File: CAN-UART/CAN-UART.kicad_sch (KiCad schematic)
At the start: 13 parts, among them P1 USB_C_Plug_USB2.0, U1 AP2112K-3.3, U2 SN65HVD230

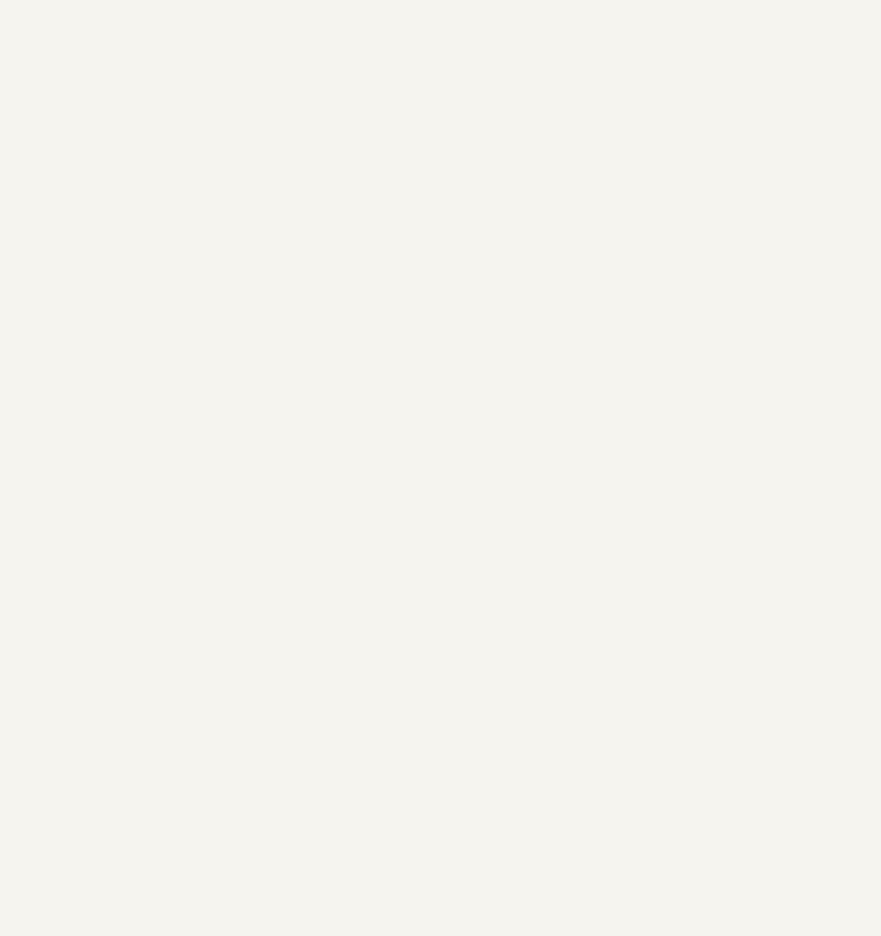
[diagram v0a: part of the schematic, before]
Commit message: Added ESP32 C3
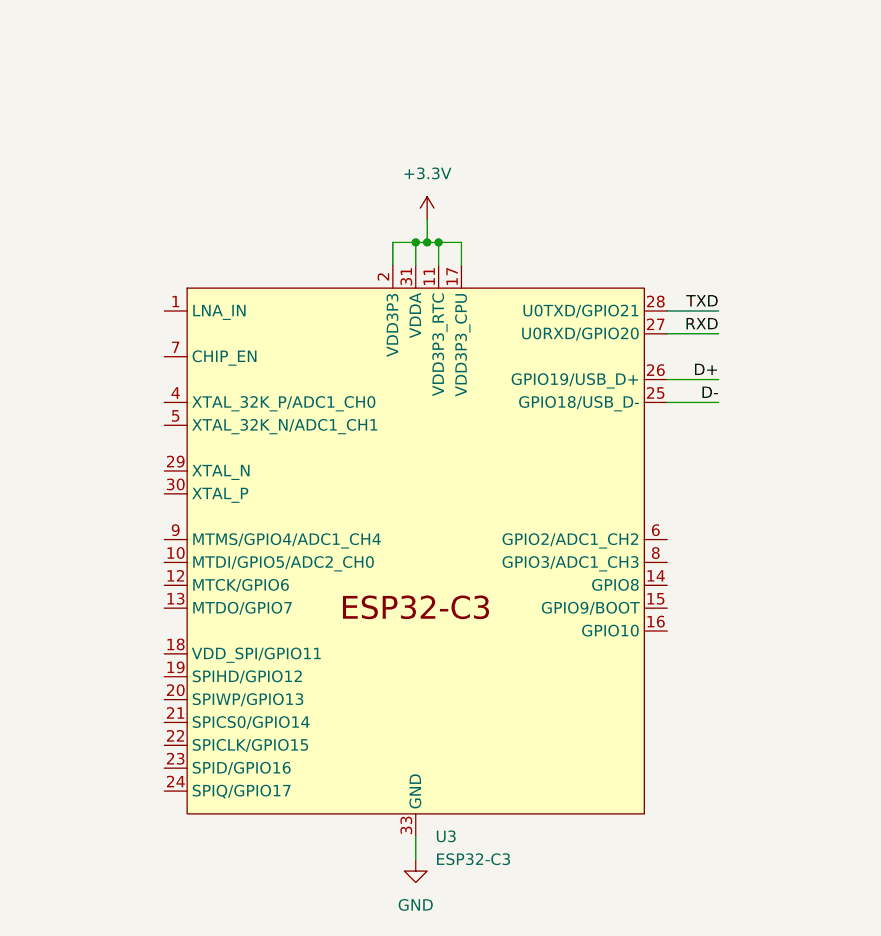
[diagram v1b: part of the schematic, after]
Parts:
- added U3: ESP32-C3, Package_DFN_QFN:QFN-32-1EP_5x5mm_P0.5mm_EP3.45x3.45mm, symbol Espressif:ESP32-C3
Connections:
- net D+: now also U3.26 (GPIO19/USB_D+)
- net D-: now also U3.25 (GPIO18/USB_D-)
- net GND: now also U3.33 (GND)
- new net +3.3V: U3.11 (VDD3P3_RTC), U3.17 (VDD3P3_CPU), U3.2 (VDD3P3), U3.3 (VDD3P3), U3.31 (VDDA), U3.32 (VDDA)
- new net RXD: U3.27 (U0RXD/GPIO20)
- new net TXD: U3.28 (U0TXD/GPIO21)
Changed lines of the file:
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@@
   (junction (at 144.78 24.13) (diameter 0) (color 0 0 0 0)
   )
+  (junction (at 120.65 96.52) (diameter 0) (color 0 0 0 0)
+  )
   (junction (at 99.06 45.72) (diameter 0) (color 0 0 0 0)
   )
@@
   (junction (at 88.9 33.02) (diameter 0) (color 0 0 0 0)
   )
+  (junction (at 121.92 96.52) (diameter 0) (color 0 0 0 0)
+  )
   (junction (at 115.57 45.72) (diameter 0) (color 0 0 0 0)
+  )
+  (junction (at 123.19 96.52) (diameter 0) (color 0 0 0 0)
   )
   (no_connect (at 322.58 104.14))
@@
     (stroke (width 0) (type default))
   )
+  (wire (pts (xy 120.65 96.52) (xy 120.65 99.06))
+    (stroke (width 0) (type default))
+  )
   (wire (pts (xy 340.36 109.22) (xy 340.36 111.76))
     (stroke (width 0) (type default))
@@
     (stroke (width 0) (type default))
   )
+  (wire (pts (xy 148.59 104.14) (xy 154.305 104.14))
+    (stroke (width 0) (type default))
+  )
+  (wire (pts (xy 118.11 96.52) (xy 120.65 96.52))
+    (stroke (width 0) (type default))
+  )
+  (wire (pts (xy 118.11 99.06) (xy 118.11 96.52))
+    (stroke (width 0) (type default))
+  )
   (wire (pts (xy 67.31 36.83) (xy 64.77 36.83))
     (stroke (width 0) (type default))
@@
     (stroke (width 0) (type default))
   )
+  (wire (pts (xy 123.19 96.52) (xy 123.19 99.06))
+    (stroke (width 0) (type default))
+  )
   (wire (pts (xy 106.68 33.02) (xy 115.57 33.02))
     (stroke (width 0) (type default))
@@
     (stroke (width 0) (type default))
   )
+  (wire (pts (xy 148.59 111.76) (xy 154.305 111.76))
+    (stroke (width 0) (type default))
+  )
   (wire (pts (xy 350.52 99.06) (xy 353.06 99.06))
     (stroke (width 0) (type default))
@@
     (stroke (width 0) (type default))
   )
+  (wire (pts (xy 120.65 96.52) (xy 121.92 96.52))
+    (stroke (width 0) (type default))
+  )
+  (wire (pts (xy 123.19 96.52) (xy 125.73 96.52))
+    (stroke (width 0) (type default))
+  )
   (wire (pts (xy 156.21 30.48) (xy 144.78 30.48))
     (stroke (width 0) (type default))
   )
+  (wire (pts (xy 125.73 96.52) (xy 125.73 99.06))
+    (stroke (width 0) (type default))
+  )
   (wire (pts (xy 67.31 36.83) (xy 67.31 39.37))
     (stroke (width 0) (type default))
@@
     (stroke (width 0) (type default))
   )
+  (wire (pts (xy 148.59 114.3) (xy 154.305 114.3))
+    (stroke (width 0) (type default))
+  )
   (wire (pts (xy 322.58 101.6) (xy 330.2 101.6))
     (stroke (width 0) (type default))
@@
     (stroke (width 0) (type default))
   )
+  (wire (pts (xy 120.65 162.56) (xy 120.65 165.1))
+    (stroke (width 0) (type default))
+  )
+  (wire (pts (xy 121.92 96.52) (xy 123.19 96.52))
+    (stroke (width 0) (type default))
+  )
   (wire (pts (xy 88.9 35.56) (xy 88.9 33.02))
     (stroke (width 0) (type default))
   )
+  (wire (pts (xy 148.59 106.68) (xy 154.305 106.68))
+    (stroke (width 0) (type default))
+  )
   (wire (pts (xy 115.57 25.4) (xy 115.57 33.02))
+    (stroke (width 0) (type default))
+  )
+  (wire (pts (xy 121.92 93.98) (xy 121.92 96.52))
     (stroke (width 0) (type default))
   )
@@
     (effects (font (size 2.54 2.54)) (justify left bottom))
   )
+  (label "D-" (at 154.305 114.3 180) (fields_autoplaced)
+    (effects (font (size 1.27 1.27)) (justify right bottom))
+  )
   (label "CAN_RX" (at 322.58 99.06 0) (fields_autoplaced)
     (effects (font (size 1.27 1.27)) (justify left bottom))
   )
   (label "D+" (at 57.15 49.53 180) (fields_autoplaced)
+    (effects (font (size 1.27 1.27)) (justify right bottom))
+  )
+  (label "RXD" (at 154.305 106.68 180) (fields_autoplaced)
+    (effects (font (size 1.27 1.27)) (justify right bottom))
+  )
+  (label "TXD" (at 154.305 104.14 180) (fields_autoplaced)
+    (effects (font (size 1.27 1.27)) (justify right bottom))
+  )
+  (label "D+" (at 154.305 111.76 180) (fields_autoplaced)
     (effects (font (size 1.27 1.27)) (justify right bottom))
   )
@@
     )
   )
+  (symbol (lib_id "Espressif:ESP32-C3") (at 120.65 132.08 0) (unit 1)
+    (in_bom yes) (on_board yes) (dnp no) (fields_autoplaced)
+    (property "Reference" "U3" (at 122.8441 162.56 0)
+      (effects (font (size 1.27 1.27)) (justify left))
+    )
+    (property "Value" "ESP32-C3" (at 122.8441 165.1 0)
+      (effects (font (size 1.27 1.27)) (justify left))
+    )
+    (property "Footprint" "Package_DFN_QFN:QFN-32-1EP_5x5mm_P0.5mm_EP3.45x3.45mm" (at 120.65 170.18 0)
+      (effects (font (size 1.27 1.27)) hide)
+    )
+    (property "Datasheet" "https://www.espressif.com/sites/default/files/documentation/esp32-c3_datasheet_en.pdf" (at 120.65 172.72 0)
+      (effects (font (size 1.27 1.27)) hide)
+    )
+    (pin "1")
+    (pin "10")
+    (pin "11")
+    (pin "12")
+    (pin "13")
+    (pin "14")
+    (pin "15")
+    (pin "16")
+    (pin "17")
+    (pin "18")
+    (pin "19")
+    (pin "2")
+    (pin "20")
+    (pin "21")
+    (pin "22")
+    (pin "23")
+    (pin "24")
+    (pin "25")
+    (pin "26")
+    (pin "27")
+    (pin "28")
+    (pin "29")
+    (pin "30")
+    (pin "31")
+    (pin "33")
+    (pin "4")
+    (pin "5")
+    (pin "6")
+    (pin "7")
+    (pin "8")
+    (pin "9")
+    (pin "3")
+    (pin "32")
+    (instances
+      (project "CAN-UART"
+        (path "/21020eba-b649-4135-9bee-384d0a5cab58"
+          (reference "U3") (unit 1)
+        )
+      )
+    )
+  )
   (symbol (lib_id "Interface_CAN_LIN:SN65HVD230") (at 340.36 99.06 0) (unit 1)
     (in_bom yes) (on_board yes) (dnp no) (fields_autoplaced)
@@
         )
       )
+    )
+  )
+  (symbol (lib_name "GND_1") (lib_id "power:GND") (at 120.65 165.1 0) (unit 1)
+    (in_bom yes) (on_board yes) (dnp no) (fields_autoplaced)
+    (property "Reference" "#PWR010" (at 120.65 171.45 0)
+      (effects (font (size 1.27 1.27)) hide)
+    )
+    (property "Value" "GND" (at 120.65 170.18 0)
+      (effects (font (size 1.27 1.27)))
+    )
+    (property "Footprint" "" (at 120.65 165.1 0)
+      (effects (font (size 1.27 1.27)) hide)
+    )
+    (property "Datasheet" "" (at 120.65 165.1 0)
+      (effects (font (size 1.27 1.27)) hide)
+    )
+    (pin "1")
+    (instances
+      (project "CAN-UART"
+        (path "/21020eba-b649-4135-9bee-384d0a5cab58"
+          (reference "#PWR010") (unit 1)
+        )
+      )
+    )
+  )
+  (symbol (lib_id "power:+3.3V") (at 121.92 93.98 0) (unit 1)
+    (in_bom yes) (on_board yes) (dnp no) (fields_autoplaced)
+    (property "Reference" "#PWR07" (at 121.92 97.79 0)
+      (effects (font (size 1.27 1.27)) hide)
+    )
+    (property "Value" "+3.3V" (at 121.92 88.9 0)
+      (effects (font (size 1.27 1.27)))
+    )
+    (property "Footprint" "" (at 121.92 93.98 0)
+      (effects (font (size 1.27 1.27)) hide)
+    )
+    (property "Datasheet" "" (at 121.92 93.98 0)
+      (effects (font (size 1.27 1.27)) hide)
+    )
+    (pin "1")
+    (instances
+      (project "CAN-UART"
+        (path "/21020eba-b649-4135-9bee-384d0a5cab58"
+          (reference "#PWR07") (unit 1)
+        )
+      )

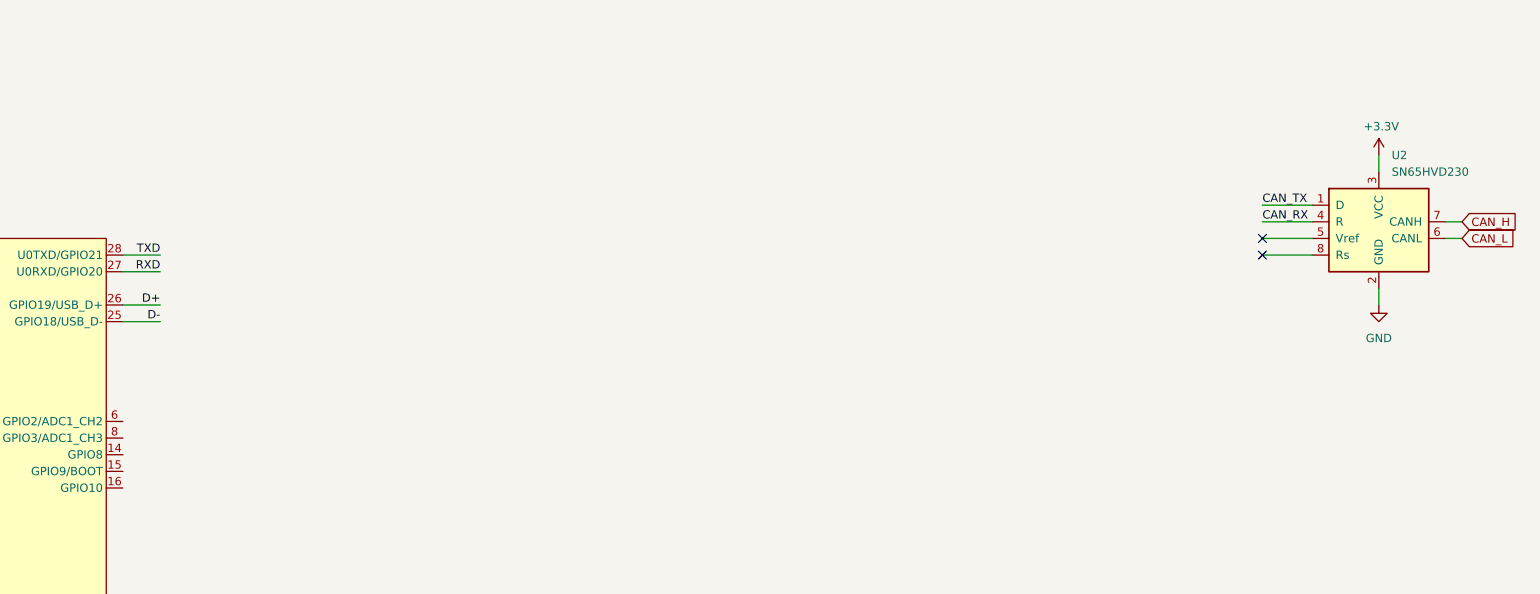
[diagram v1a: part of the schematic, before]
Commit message: Added SN65HVD230 Transceiver
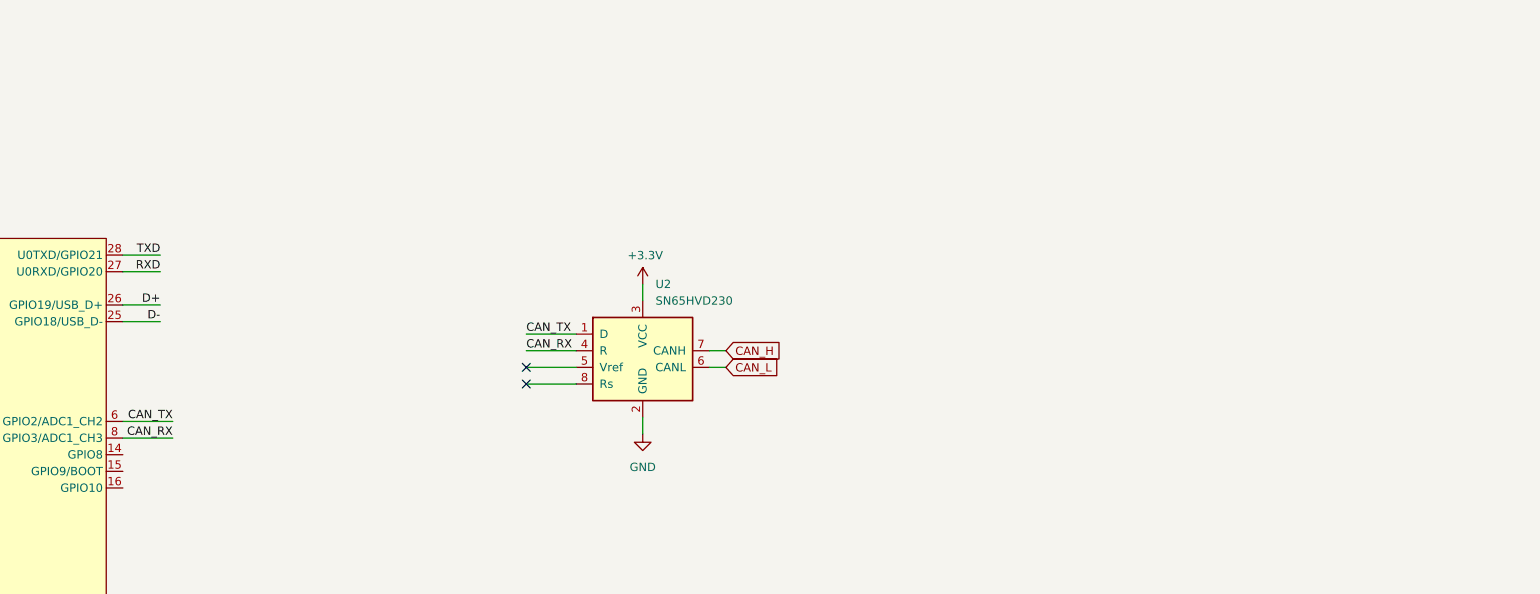
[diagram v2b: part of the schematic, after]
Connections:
- net CAN_RX: now also U3.8 (GPIO3/ADC1_CH3)
- net CAN_TX: now also U3.6 (GPIO2/ADC1_CH2)
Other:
- moved on the sheet: U2
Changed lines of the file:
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@@
   (junction (at 123.19 96.52) (diameter 0) (color 0 0 0 0)
   )
-  (no_connect (at 322.58 104.14))
+  (no_connect (at 210.185 123.825))
   (no_connect (at 57.15 39.37))
-  (no_connect (at 322.58 101.6))
+  (no_connect (at 210.185 121.285))
   (wire (pts (xy 139.7 24.13) (xy 139.7 30.48))
     (stroke (width 0) (type default))
   )
-  (wire (pts (xy 322.58 99.06) (xy 330.2 99.06))
+  (wire (pts (xy 210.185 118.745) (xy 217.805 118.745))
     (stroke (width 0) (type default))
   )
@@
     (stroke (width 0) (type default))
   )
+  (wire (pts (xy 156.21 129.54) (xy 148.59 129.54))
+    (stroke (width 0) (type default))
+  )
   (wire (pts (xy 52.07 36.83) (xy 57.15 36.83))
     (stroke (width 0) (type default))
@@
     (stroke (width 0) (type default))
   )
-  (wire (pts (xy 340.36 109.22) (xy 340.36 111.76))
-    (stroke (width 0) (type default))
-  )
-  (wire (pts (xy 340.36 88.9) (xy 340.36 91.44))
+  (wire (pts (xy 227.965 128.905) (xy 227.965 131.445))
+    (stroke (width 0) (type default))
+  )
+  (wire (pts (xy 227.965 108.585) (xy 227.965 111.125))
     (stroke (width 0) (type default))
   )
@@
     (stroke (width 0) (type default))
   )
+  (wire (pts (xy 156.21 132.08) (xy 148.59 132.08))
+    (stroke (width 0) (type default))
+  )
   (wire (pts (xy 36.83 72.39) (xy 36.83 69.85))
     (stroke (width 0) (type default))
   )
-  (wire (pts (xy 350.52 101.6) (xy 353.06 101.6))
+  (wire (pts (xy 238.125 121.285) (xy 240.665 121.285))
     (stroke (width 0) (type default))
   )
@@
     (stroke (width 0) (type default))
   )
-  (wire (pts (xy 322.58 104.14) (xy 330.2 104.14))
+  (wire (pts (xy 210.185 123.825) (xy 217.805 123.825))
     (stroke (width 0) (type default))
   )
@@
     (stroke (width 0) (type default))
   )
-  (wire (pts (xy 350.52 99.06) (xy 353.06 99.06))
+  (wire (pts (xy 238.125 118.745) (xy 240.665 118.745))
     (stroke (width 0) (type default))
   )
@@
     (stroke (width 0) (type default))
   )
-  (wire (pts (xy 322.58 96.52) (xy 330.2 96.52))
+  (wire (pts (xy 210.185 116.205) (xy 217.805 116.205))
     (stroke (width 0) (type default))
   )
@@
     (stroke (width 0) (type default))
   )
-  (wire (pts (xy 322.58 101.6) (xy 330.2 101.6))
+  (wire (pts (xy 210.185 121.285) (xy 217.805 121.285))
     (stroke (width 0) (type default))
   )
@@
     (effects (font (size 1.27 1.27)) (justify right bottom))
   )
-  (label "CAN_RX" (at 322.58 99.06 0) (fields_autoplaced)
+  (label "CAN_RX" (at 210.185 118.745 0) (fields_autoplaced)
     (effects (font (size 1.27 1.27)) (justify left bottom))
   )
@@
     (effects (font (size 1.27 1.27)) (justify right bottom))
   )
-  (label "CAN_TX" (at 322.58 96.52 0) (fields_autoplaced)
+  (label "CAN_TX" (at 210.185 116.205 0) (fields_autoplaced)
     (effects (font (size 1.27 1.27)) (justify left bottom))
   )
@@
     (effects (font (size 1.27 1.27)) (justify right bottom))
   )
-  (global_label "CAN_H" (shape input) (at 353.06 99.06 0) (fields_autoplaced)
+  (label "CAN_TX" (at 156.21 129.54 180) (fields_autoplaced)
+    (effects (font (size 1.27 1.27)) (justify right bottom))
+  )
+  (label "CAN_RX" (at 156.21 132.08 180) (fields_autoplaced)
+    (effects (font (size 1.27 1.27)) (justify right bottom))
+  )
+  (global_label "CAN_H" (shape input) (at 240.665 118.745 0) (fields_autoplaced)
     (effects (font (size 1.27 1.27)) (justify left))
-    (property "Intersheetrefs" "${INTERSHEET_REFS}" (at 361.953 99.06 0)
+    (property "Intersheetrefs" "${INTERSHEET_REFS}" (at 249.558 118.745 0)
       (effects (font (size 1.27 1.27)) (justify left) hide)
     )
   )
-  (global_label "CAN_L" (shape input) (at 353.06 101.6 0) (fields_autoplaced)
+  (global_label "CAN_L" (shape input) (at 240.665 121.285 0) (fields_autoplaced)
     (effects (font (size 1.27 1.27)) (justify left))
-    (property "Intersheetrefs" "${INTERSHEET_REFS}" (at 361.6506 101.6 0)
+    (property "Intersheetrefs" "${INTERSHEET_REFS}" (at 249.2556 121.285 0)
       (effects (font (size 1.27 1.27)) (justify left) hide)
     )
@@
     )
   )
-  (symbol (lib_id "Interface_CAN_LIN:SN65HVD230") (at 340.36 99.06 0) (unit 1)
+  (symbol (lib_id "Interface_CAN_LIN:SN65HVD230") (at 227.965 118.745 0) (unit 1)
     (in_bom yes) (on_board yes) (dnp no) (fields_autoplaced)
-    (property "Reference" "U2" (at 342.3159 88.9 0)
-      (effects (font (size 1.27 1.27)) (justify left))
-    )
-    (property "Value" "SN65HVD230" (at 342.3159 91.44 0)
-      (effects (font (size 1.27 1.27)) (justify left))
-    )
-    (property "Footprint" "Package_SO:SOIC-8_3.9x4.9mm_P1.27mm" (at 340.36 111.76 0)
-      (effects (font (size 1.27 1.27)) hide)
-    )
-    (property "Datasheet" "http://www.ti.com/lit/ds/symlink/sn65hvd230.pdf" (at 337.82 88.9 0)
+    (property "Reference" "U2" (at 229.9209 108.585 0)
+      (effects (font (size 1.27 1.27)) (justify left))
+    )
+    (property "Value" "SN65HVD230" (at 229.9209 111.125 0)
+      (effects (font (size 1.27 1.27)) (justify left))
+    )
+    (property "Footprint" "Package_SO:SOIC-8_3.9x4.9mm_P1.27mm" (at 227.965 131.445 0)
+      (effects (font (size 1.27 1.27)) hide)
+    )
+    (property "Datasheet" "http://www.ti.com/lit/ds/symlink/sn65hvd230.pdf" (at 225.425 108.585 0)
       (effects (font (size 1.27 1.27)) hide)
     )
@@
     )
   )
-  (symbol (lib_name "GND_2") (lib_id "power:GND") (at 340.36 111.76 0) (unit 1)
+  (symbol (lib_name "GND_2") (lib_id "power:GND") (at 227.965 131.445 0) (unit 1)
     (in_bom yes) (on_board yes) (dnp no) (fields_autoplaced)
-    (property "Reference" "#PWR09" (at 340.36 118.11 0)
-      (effects (font (size 1.27 1.27)) hide)
-    )
-    (property "Value" "GND" (at 340.36 116.84 0)
-      (effects (font (size 1.27 1.27)))
-    )
-    (property "Footprint" "" (at 340.36 111.76 0)
-      (effects (font (size 1.27 1.27)) hide)
-    )
-    (property "Datasheet" "" (at 340.36 111.76 0)
+    (property "Reference" "#PWR09" (at 227.965 137.795 0)
+      (effects (font (size 1.27 1.27)) hide)
+    )
+    (property "Value" "GND" (at 227.965 136.525 0)
+      (effects (font (size 1.27 1.27)))
+    )
+    (property "Footprint" "" (at 227.965 131.445 0)
+      (effects (font (size 1.27 1.27)) hide)
+    )
+    (property "Datasheet" "" (at 227.965 131.445 0)
       (effects (font (size 1.27 1.27)) hide)
     )
@@
     )
   )
-  (symbol (lib_id "Expansion_Card-rescue:+3.3V-power") (at 340.36 88.9 0) (unit 1)
-    (in_bom yes) (on_board yes) (dnp no)
-    (property "Reference" "#PWR08" (at 340.36 92.71 0)
-      (effects (font (size 1.27 1.27)) hide)
-    )
-    (property "Value" "+3.3V" (at 340.741 84.5058 0)
-      (effects (font (size 1.27 1.27)))
-    )
-    (property "Footprint" "" (at 340.36 88.9 0)
-      (effects (font (size 1.27 1.27)) hide)
-    )
-    (property "Datasheet" "" (at 340.36 88.9 0)
-      (effects (font (size 1.27 1.27)) hide)
-    )
+  (symbol (lib_id "Expansion_Card-rescue:+3.3V-power") (at 227.965 108.585 0) (unit 1)
+    (in_bom yes) (on_board yes) (dnp no)
+    (property "Reference" "#PWR08" (at 227.965 112.395 0)
+      (effects (font (size 1.27 1.27)) hide)
+    )
+    (property "Value" "+3.3V" (at 228.346 104.1908 0)
+      (effects (font (size 1.27 1.27)))
+    )
+    (property "Footprint" "" (at 227.965 108.585 0)
+      (effects (font (size 1.27 1.27)) hide)
+    )
+    (property "Datasheet" "" (at 227.965 108.585 0)
+      (effects (font (size 1.27 1.27)) hide)
+    )
